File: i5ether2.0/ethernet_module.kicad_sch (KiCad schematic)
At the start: 14 parts, among them J2 Conn_02x05_Odd_Even, J3 1-406541-1, T2 HX5008

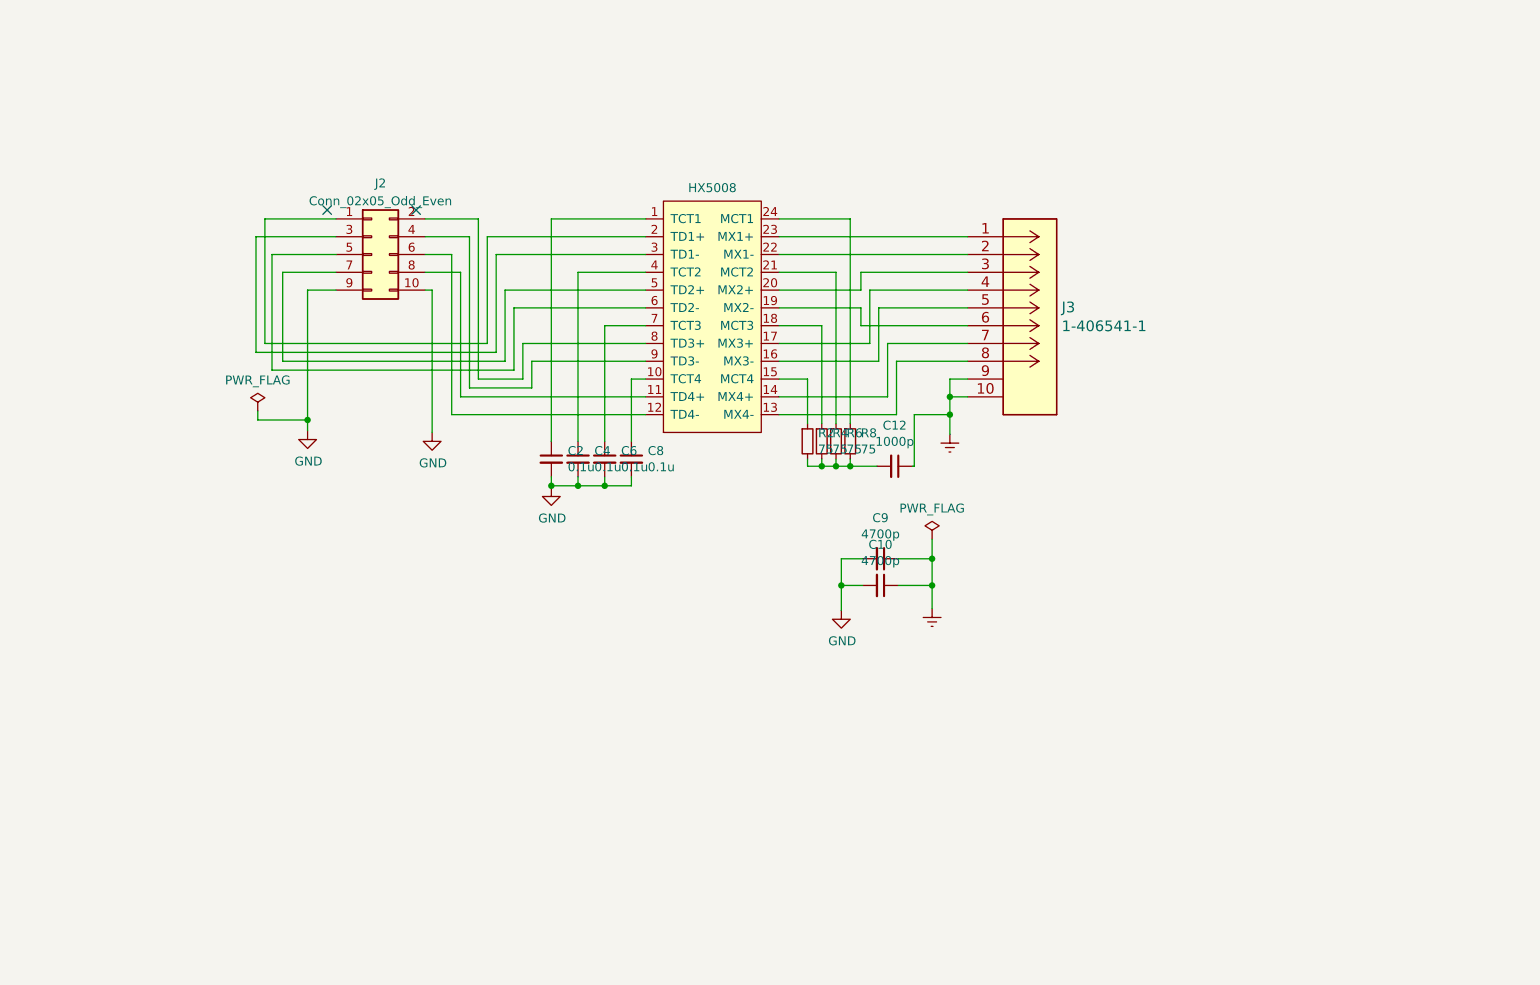
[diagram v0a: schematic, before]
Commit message: Arreglos esquematico ethernet
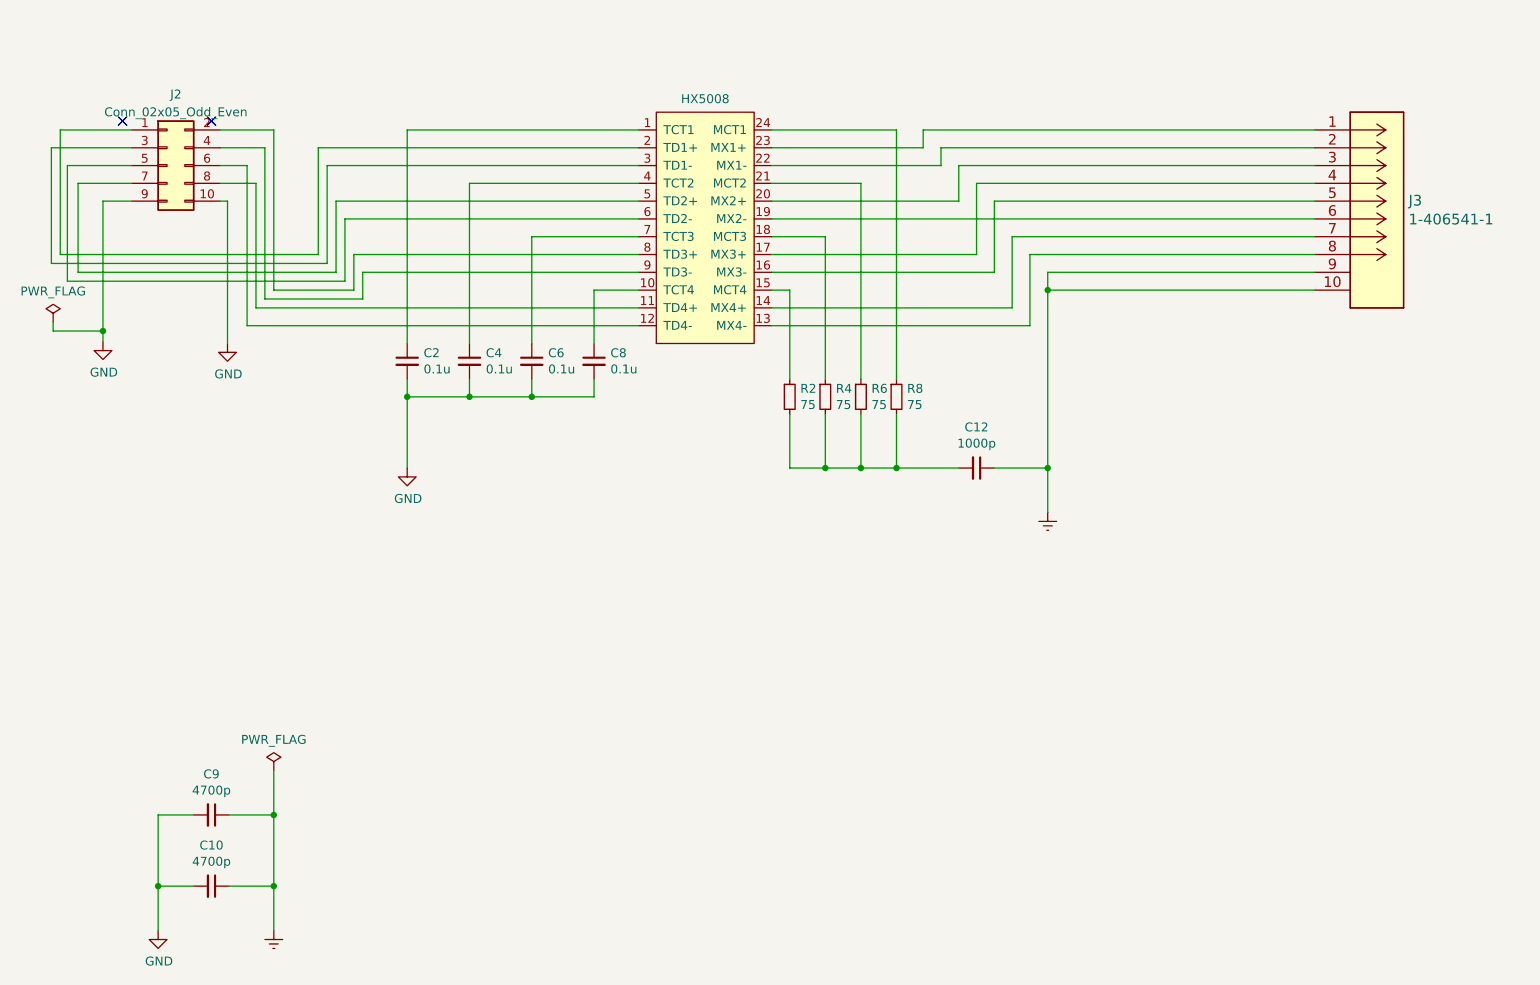
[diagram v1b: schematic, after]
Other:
- moved on the sheet: C10, C12, C2, C4, C6, C8, C9, J2, J3, R2, R4, R6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

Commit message: Essquematico con pantalla
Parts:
- removed J2: Conn_02x05_Odd_Even, Connector_PinHeader_2.54mm:PinHeader_2x05_P2.54mm_Vertical, symbol Connector_Generic:Conn_02x05_Odd_Even
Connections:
- net TD1+: now reaches T2.2 (TD1+)
- net TD3+: now reaches T2.8 (TD3+)
- net TD1-: now reaches T2.3 (TD1-)
- net TD3-: now reaches T2.9 (TD3-)
- net TD2-: now reaches T2.6 (TD2-)
- net TD4-: now reaches T2.12 (TD4-)
- net TD2+: now reaches T2.5 (TD2+)
- net TD4+: now reaches T2.11 (TD4+)
- no-connect marks 2 -> 0
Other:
- moved on the sheet: C10, C2, C4, C6, C8, C9

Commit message: Avances en placa
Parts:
- removed C10, C9: 4700p, Resistor_SMD:R_1812_4532Metric, symbol Device:C_Small
- removed C12: 1000p, Capacitor_SMD:C_0402_1005Metric, symbol Device:C_Small
- removed C2, C4, C6, C8: 0.1u, Capacitor_SMD:C_0402_1005Metric, symbol Device:C_Small
- removed J3: 1-406541-1, MJ406541:1-406541-1, symbol MJ406541:1-406541-1
- removed R2, R4, R6, R8: 75, Resistor_SMD:R_0402_1005Metric, symbol Device:R_Small
- removed T2: HX5008, HX5008:HX5008NL, symbol HX5008:HX5008
- added J2: 7499011121A, KiCad:7499011121A, symbol 7499011121A:7499011121A
- added R1, R2, R3, R4: 50, symbol Device:R
- added R5, R6: 330, symbol Device:R
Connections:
- new net: J2.12, R6.1
- new net: J2.10, R5.1
- new net +3.3V: J2.11, J2.2, J2.5, J2.9, R1.1, R2.1, R3.1, R4.1
- new net GLED-: R6.2
- new net RD+: J2.4, R3.2
- new net RD-: J2.6, R4.2
- new net TD+: J2.1, R1.2
- new net TD-: J2.3, R2.2
- new net YLED-: R5.2
- no-connect marks 0 -> 4
